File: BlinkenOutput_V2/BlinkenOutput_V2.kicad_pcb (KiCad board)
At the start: 2 copper layers, 72.2 x 45.8 mm, 27 parts, among them J1 Conn_01x10, J2 Conn_01x10, J3 Conn_02x07_Odd_Even, J4 Conn_02x02_Counter_Clockwise, J5 Conn_02x02_Counter_Clockwise, U1 LTV-847S, U2 LTV-847S, U3 74HC595, U4 74LVC1G125

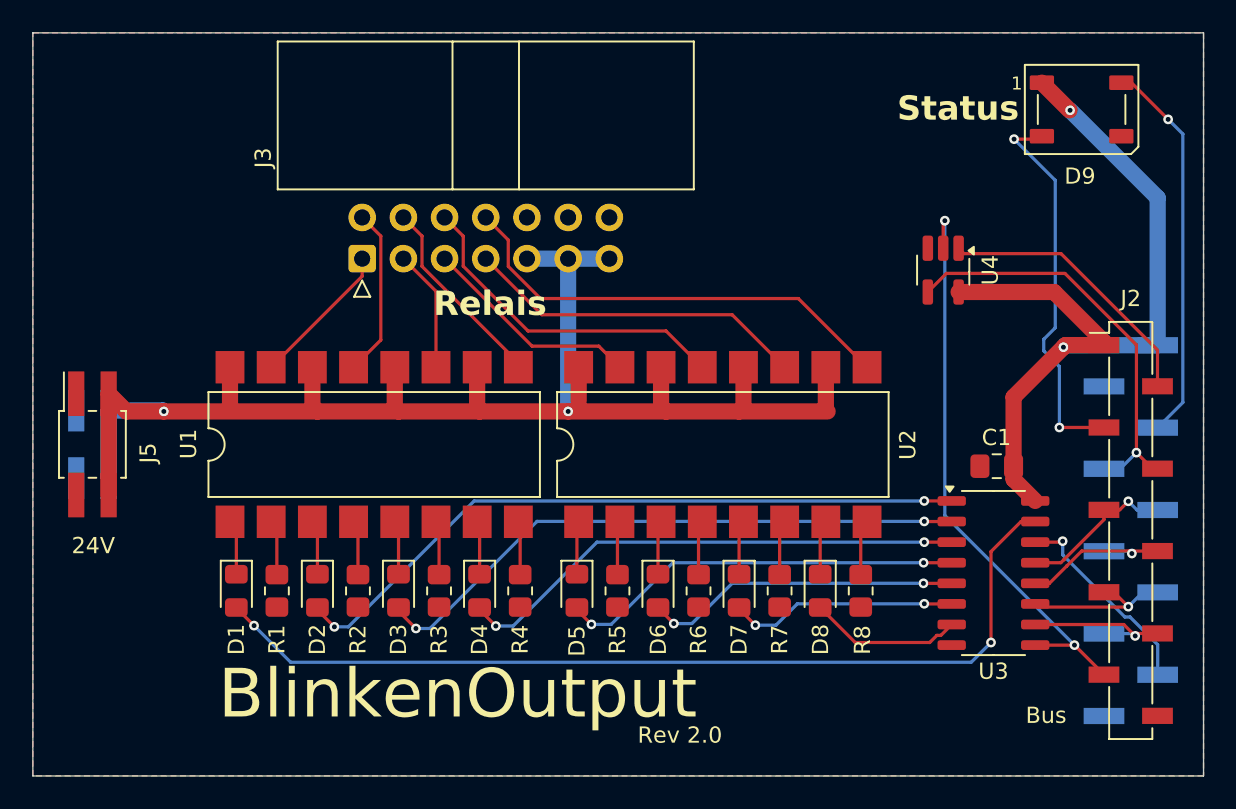
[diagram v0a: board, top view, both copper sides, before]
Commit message: Overhauled the output board
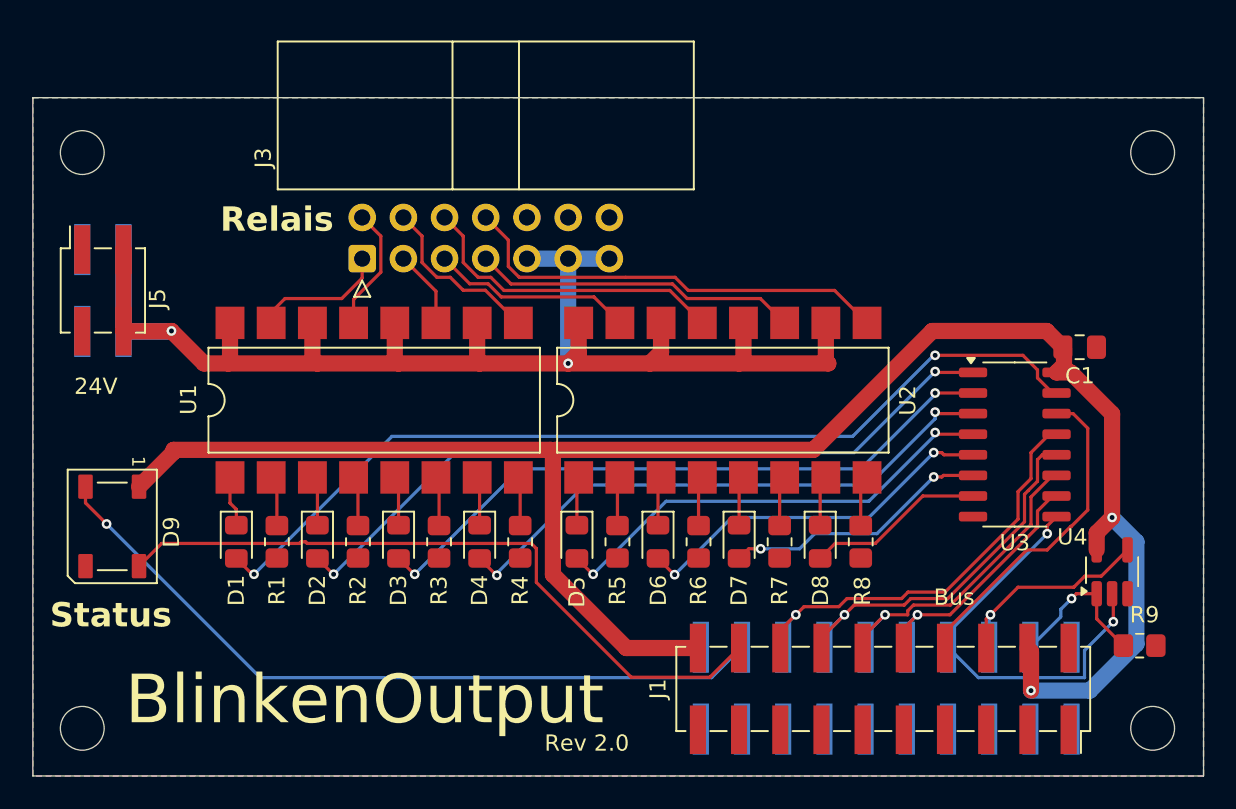
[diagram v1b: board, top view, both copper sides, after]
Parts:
- added R9: 10k, Resistor_SMD:R_0805_2012Metric_Pad1.20x1.40mm_HandSolder, F.Cu at (182.7, 67.4)
- added REF**: MountingHole_2.7mm_M2.5, MountingHole:MountingHole_2.7mm_M2.5, F.Cu at (117.5, 37.0)
- added REF**: MountingHole_2.7mm_M2.5, MountingHole:MountingHole_2.7mm_M2.5, F.Cu at (117.5, 72.5)
- added REF**: MountingHole_2.7mm_M2.5, MountingHole:MountingHole_2.7mm_M2.5, F.Cu at (183.5, 72.5)
- added REF**: MountingHole_2.7mm_M2.5, MountingHole:MountingHole_2.7mm_M2.5, F.Cu at (183.5, 37.0)
- J1: value Conn_01x10 -> Conn_02x10_Odd_Even; footprint Connector_PinHeader_2.54mm:PinHeader_1x10_P2.54mm_Vertical_SMD_Pin1Left -> Connector_PinSocket_2.54mm:PinSocket_2x10_P2.54mm_Vertical_SMD; moved to F.Cu
- J2: value Conn_01x10 -> Conn_02x10_Odd_Even; footprint Connector_PinSocket_2.54mm:PinSocket_1x10_P2.54mm_Vertical_SMD_Pin1Left -> Connector_PinHeader_2.54mm:PinHeader_2x10_P2.54mm_Vertical_SMD; moved to B.Cu
- J4: footprint Connector_PinHeader_2.00mm:PinHeader_2x02_P2.00mm_Vertical_SMD -> Connector_PinHeader_2.54mm:PinHeader_2x02_P2.54mm_Vertical_SMD
- J5: footprint Connector_PinSocket_2.00mm:PinSocket_2x02_P2.00mm_Vertical_SMD -> Connector_PinSocket_2.54mm:PinSocket_2x02_P2.54mm_Vertical_SMD
- moved D9 65.1 mm to (119.3, 60.0), turned to -90 degrees
- moved U4 21.3 mm to (181.0, 62.9), turned to 90 degrees
- moved J1 18.1 mm to (166.9, 70.1), turned to -90 degrees
- moved J2 17.9 mm to (167.1, 70.0), turned to 90 degrees
- moved J5 9.51 mm to (118.8, 45.5)
- moved J4 9.51 mm to (118.8, 45.5)
- moved C1 8.94 mm to (179.0, 49.0), turned to 0 degrees
- moved U3 8.03 mm to (175.0, 55.0)
- moved D1 3.03 mm to (127.0, 61.0)
- moved D2 3.03 mm to (132.0, 61.0)
- moved D3 3.03 mm to (137.0, 61.0)
- moved D4 3.03 mm to (142.0, 61.0)
- moved D5 3.03 mm to (148.0, 61.0)
- moved D6 3.03 mm to (153.0, 61.0)
- moved D7 3.03 mm to (158.0, 61.0)
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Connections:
- J1 pad 1: GND -> unconnected-(J1-Pin_1-Pad1)
- J1 pad 10: VCC -> Reset
- J1 pad 2: Data -> GND
- J1 pad 3: Reset -> unconnected-(J1-Pin_3-Pad3)
- J1 pad 4: Clock -> VCC
- J1 pad 5: Strobe -> unconnected-(J1-Pin_5-Pad5)
- J1 pad 6: Output Enable -> Return
- J1 pad 7: Return -> unconnected-(J1-Pin_7-Pad7)
- J1 pad 8: Led IN -> Data
- J1 pad 9: GND -> unconnected-(J1-Pin_9-Pad9)
- J2 pad 1: VCC -> unconnected-(J2-Pin_1-Pad1)
- J2 pad 10: GND -> Reset
- J2 pad 2: Sense -> GND
- J2 pad 3: Led OUT -> unconnected-(J2-Pin_3-Pad3)
- J2 pad 4: Return -> Sense
- J2 pad 5: Output Enable -> unconnected-(J2-Pin_5-Pad5)
- J2 pad 6: Strobe -> Return
- J2 pad 7: Clock -> unconnected-(J2-Pin_7-Pad7)
- J2 pad 8: Reset -> Data Out
- J2 pad 9: Data Out -> unconnected-(J2-Pin_9-Pad9)
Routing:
- net VCC: track 50.0 -> 113.8 mm
- net Led OUT: track 24.1 -> 46.7 mm, vias 2 -> 1
- net Led IN: track 23.9 -> 43.0 mm, vias 1 -> 0
- net Output Enable: track 9.70 -> 27.4 mm
- net Strobe: track 10.3 -> 24.1 mm
- net Return: track 26.3 -> 14.3 mm
- net Clock: track 9.87 -> 20.4 mm
- net Data Out: track 36.3 -> 26.0 mm
- net Data: track 12.6 -> 20.2 mm, vias 1 -> 0
- net Reset: track 9.88 -> 16.9 mm
- net Sense: track 17.1 -> 10.3 mm, vias 0 -> 1
- net +24V: track 94.6 -> 89.0 mm
- net Net-(D5-A): track 25.2 -> 28.7 mm
- net Net-(D6-A): track 19.6 -> 23.0 mm
- net Net-(D4-A): track 32.0 -> 35.4 mm
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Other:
- board size 72.2 x 45.8 mm -> 72.2 x 41.8 mm
- board text added: "GND"
